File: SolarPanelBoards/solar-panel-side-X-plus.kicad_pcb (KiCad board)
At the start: 2 copper layers, 82 x 99 mm, 24 parts, among them J1 Conn_01x06, U1 OPT3001DNPT

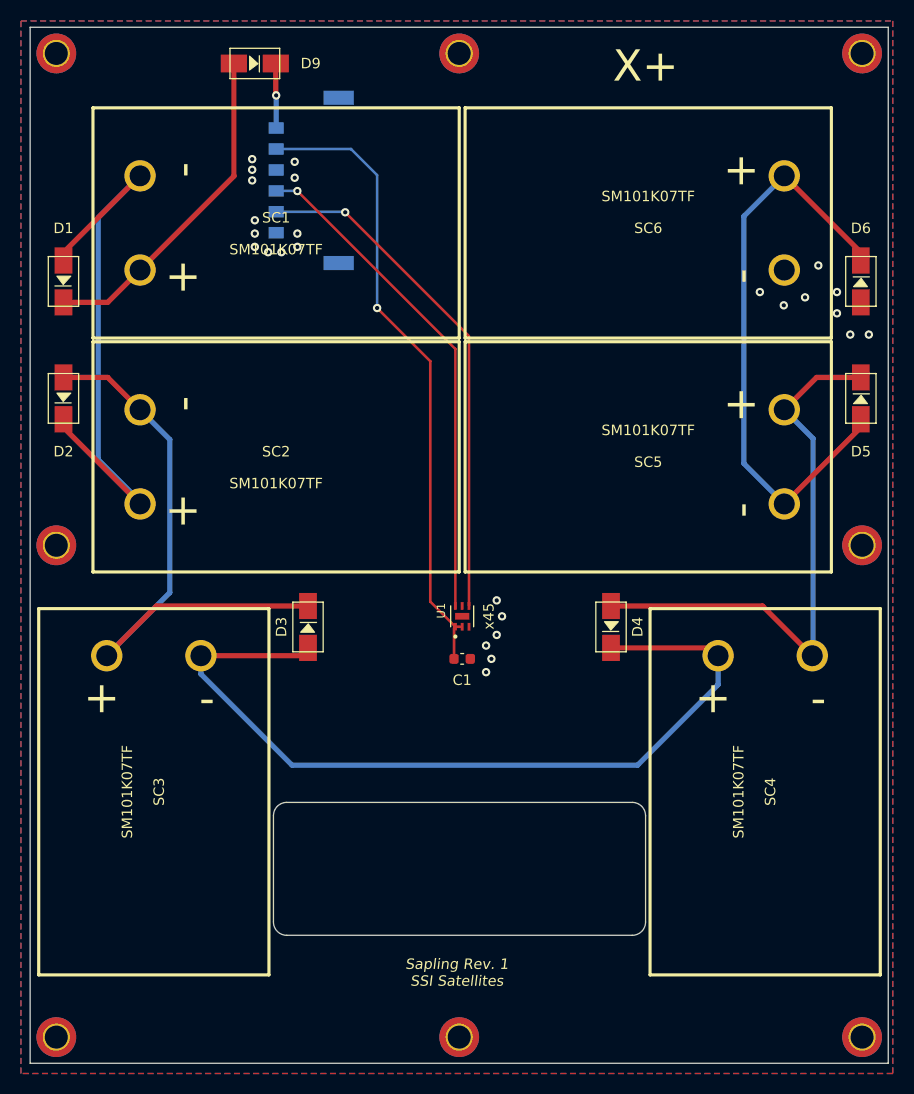
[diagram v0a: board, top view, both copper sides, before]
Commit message: Updated X-plus schematic, netlist, PCB, and gerbers
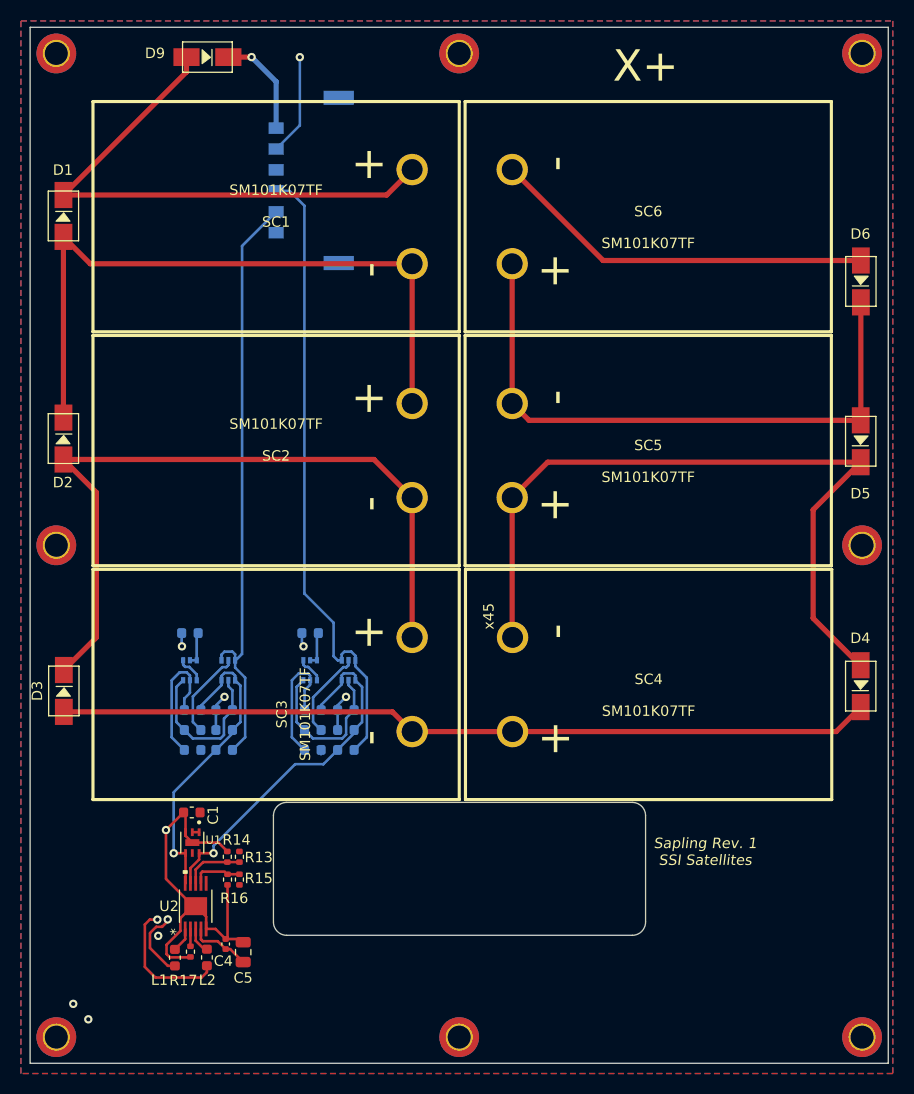
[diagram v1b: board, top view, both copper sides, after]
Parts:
- added C2: 10nF, Capacitor_SMD:C_0603_1608Metric, F.Cu at (112.9, 114.4)
- added C3: 10nF, Capacitor_SMD:C_0603_1608Metric, F.Cu at (124.4, 114.4)
- added C4: 0.1uF, Capacitor_SMD:C_0402_1005Metric, F.Cu at (116.1, 132.9)
- added C5: 10uF, Capacitor_SMD:C_0805_2012Metric, F.Cu at (117.8, 133.7)
- added L1: TBD, Inductor_SMD:L_0603_1608Metric, F.Cu at (111.2, 134.2)
- added L2: TBD, Inductor_SMD:L_0603_1608Metric, F.Cu at (114.3, 134.2)
- added Q1: MBT2222ADW1T1, Package_TO_SOT_SMD:SOT-363_SC-70-6, F.Cu at (116.3, 106.8)
- added Q2: MBT2222ADW1T1, Package_TO_SOT_SMD:SOT-363_SC-70-6, F.Cu at (127.8, 106.8)
- added Q3: BSS138DWQ-7, mainboard:BSS138DWQ-7, F.Cu at (112.7, 106.8)
- added Q4: BSS138DWQ-7, mainboard:BSS138DWQ-7, F.Cu at (124.2, 106.8)
- added R1: 10K, Resistor_SMD:R_0603_1608Metric, F.Cu at (115.9, 110.6)
- added R10: 100K, Resistor_SMD:R_0603_1608Metric, F.Cu at (124.4, 110.6)
- added R11: 0, Resistor_SMD:R_0603_1608Metric, F.Cu at (115.9, 114.4)
- added R12: 0, Resistor_SMD:R_0603_1608Metric, F.Cu at (127.6, 114.4)
- added R13: 0, Resistor_SMD:R_0402_1005Metric, F.Cu at (117.4, 124.6)
- added R14: 0, Resistor_SMD:R_0402_1005Metric, F.Cu at (116.2, 124.6)
- added R15: 0, Resistor_SMD:R_0402_1005Metric, F.Cu at (117.4, 126.8)
- added R16: 0, Resistor_SMD:R_0402_1005Metric, F.Cu at (116.3, 126.8)
- added R17: 0, Resistor_SMD:R_0402_1005Metric, F.Cu at (112.7, 133.6)
- added R2: 10K, Resistor_SMD:R_0603_1608Metric, F.Cu at (127.6, 110.6)
- added R3: 10K, Resistor_SMD:R_0603_1608Metric, F.Cu at (115.9, 112.5)
- added R4: 10K, Resistor_SMD:R_0603_1608Metric, F.Cu at (127.6, 112.5)
- added R5: 600, Resistor_SMD:R_0603_1608Metric, F.Cu at (112.9, 112.5)
- added R6: 600, Resistor_SMD:R_0603_1608Metric, F.Cu at (124.4, 112.5)
- added R7: 10K, Resistor_SMD:R_0603_1608Metric, F.Cu at (112.7, 103.2)
- added R8: 10K, Resistor_SMD:R_0603_1608Metric, F.Cu at (124.2, 103.2)
- added R9: 100K, Resistor_SMD:R_0603_1608Metric, B.Cu at (112.9, 110.6)
- added U2: DRV8830DGQR, sapling:DRV8830DGQ, F.Cu at (113.2, 129.3)
- J1: moved to F.Cu
- moved U1 33.7 mm to (112.9, 123.2), turned to -90 degrees
- moved C1 29.7 mm to (112.8, 120.3), turned to 180 degrees
- moved D4 24.5 mm to (176.8, 108.3)
- moved D3 24.1 mm to (100.6, 108.7)
- moved SC3 15.5 mm to (120.9, 108.1), turned to 0 degrees
- moved SC4 15.1 mm to (156.5, 108.1), turned to 180 degrees
- moved D1 6.26 mm to (100.6, 63.3), turned to -90 degrees
- moved D9 4.57 mm to (114.3, 48.2)
- moved D5 4.10 mm to (176.8, 84.9), turned to 90 degrees
- moved D2 3.84 mm to (100.6, 84.6), turned to -90 degrees
- moved SC1 0.60 mm to (120.9, 63.4), turned to 0 degrees
- moved SC2 0.60 mm to (120.9, 85.8), turned to 0 degrees
- moved SC5 0.60 mm to (156.5, 85.8), turned to 180 degrees
- moved SC6 0.60 mm to (156.5, 63.4), turned to 180 degrees
- turned D6 to 90 degrees
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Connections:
- J1 pad 4: SDA -> SDA1_b4iso
- J1 pad 5: SCL -> SCL1_b4iso
- J1 pad S1: (no net) -> unconnected-(J1-PadS1)
- J1 pad S2: (no net) -> unconnected-(J1-PadS2)
- U1 pad 5: (no net) -> unconnected-(U1-Pad5)
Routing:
- net /torque-coil: track 0.00 -> 26027.8 mm, vias 0 -> 5
- net GND: track 0.00 -> 81.1 mm, vias 26 -> 1
- net SDA1_b4iso: track 0.00 -> 60.5 mm
- net SCL1_b4iso: track 0.00 -> 56.6 mm
- net +3V3: track 60.7 -> 25.5 mm, vias 1 -> 5
- net Net-(D1-Pad1): track 32.1 -> 52.4 mm
- net SCL: track 49.1 -> 29.5 mm
- net Net-(D4-Pad2): track 54.5 -> 71.3 mm
- net Net-(Q2-Pad5): track 0.00 -> 15.5 mm
- net Net-(Q1-Pad5): track 0.00 -> 15.3 mm
- net Net-(D2-Pad2): track 57.0 -> 70.9 mm
- net SDA: track 47.9 -> 34.9 mm
- net Net-(C2-Pad1): track 0.00 -> 12.9 mm
- net Net-(C3-Pad1): track 0.00 -> 12.7 mm
- net Net-(Q2-Pad2): track 0.00 -> 8.89 mm
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- added copper zone on F.Cu, net +3V3
- removed copper zone on F.Cu, net GND
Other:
- copper layers 2 -> 6
- net class Default removed
- board text added: "BYP"
- board text added: "DNP"
